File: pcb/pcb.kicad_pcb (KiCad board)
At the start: 2 copper layers, 60 x 30 mm, 54 parts, among them J1 USB_B_Mini, J2 I2C_BUS, J4 UART_BUS, Q1 BSS138DW-7-F, Q2 BSS138DW-7-F, SW1 PTS645Vx83, SW2 PTS645Vx83, SW3 PTS645Vx83, SW4 KMR2, U1 AP2112K-3.3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

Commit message: WIP
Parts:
- moved C6 0.80 mm to (58.8, 81.8)
- moved R14 0.80 mm to (60.8, 81.8)
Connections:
- U5 pad 10: nFAC_RST -> (no net)
- U5 pad 14: nINT -> (no net)
- U5 pad 17: (no net) -> nINT
- U5 pad 5: (no net) -> nFAC_RST
- U5 pad 6: (no net) -> RGB_LED
- U5 pad 9: RGB_LED -> (no net)
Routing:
- net UART_RX: track 55.2 -> 0.00 mm, vias 2 -> 0
- net UART_TX: track 53.3 -> 0.00 mm, vias 2 -> 0
- net nFAC_RST: track 11.3 -> 23.5 mm
- net nINT: track 12.1 -> 0.96 mm
- net RGB_LED: track 8.59 -> 15.3 mm, vias 0 -> 2

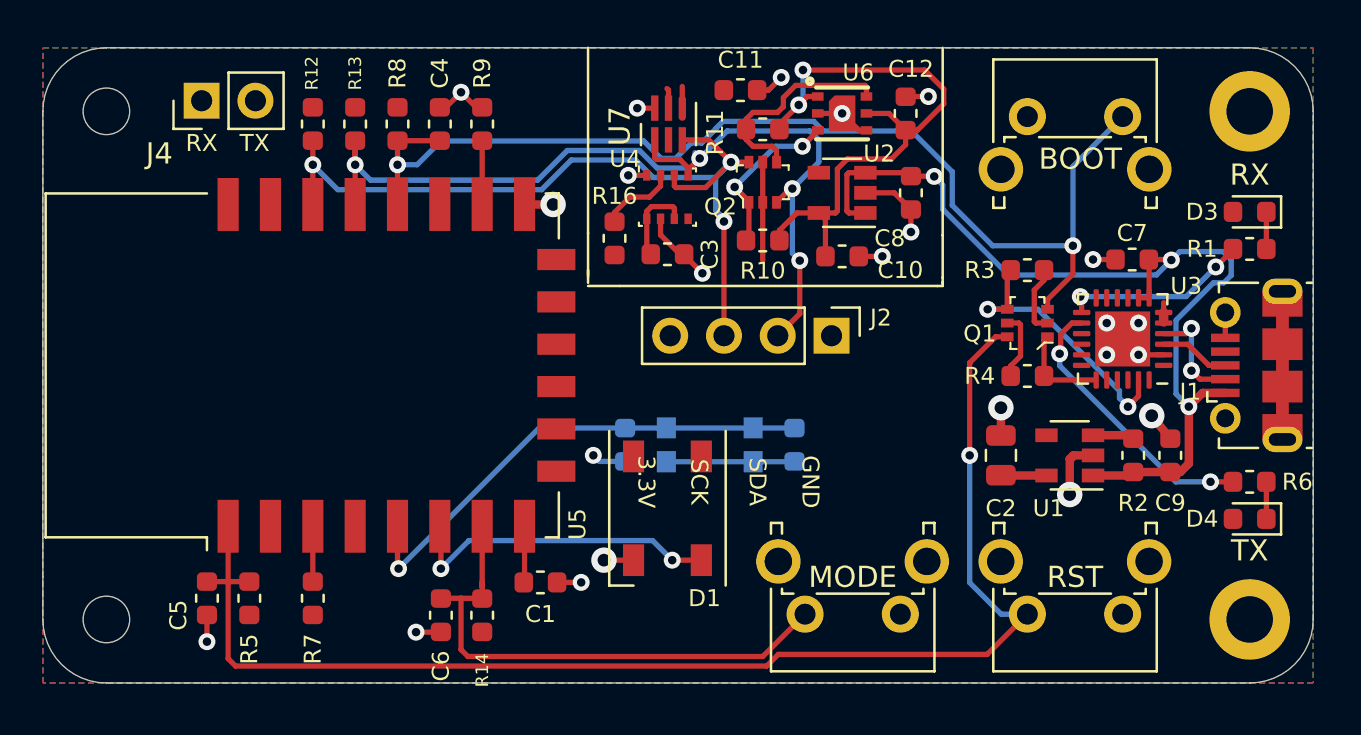
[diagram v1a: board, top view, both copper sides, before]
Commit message: Update the gerbers for the rem v1 and reroute the UART lines
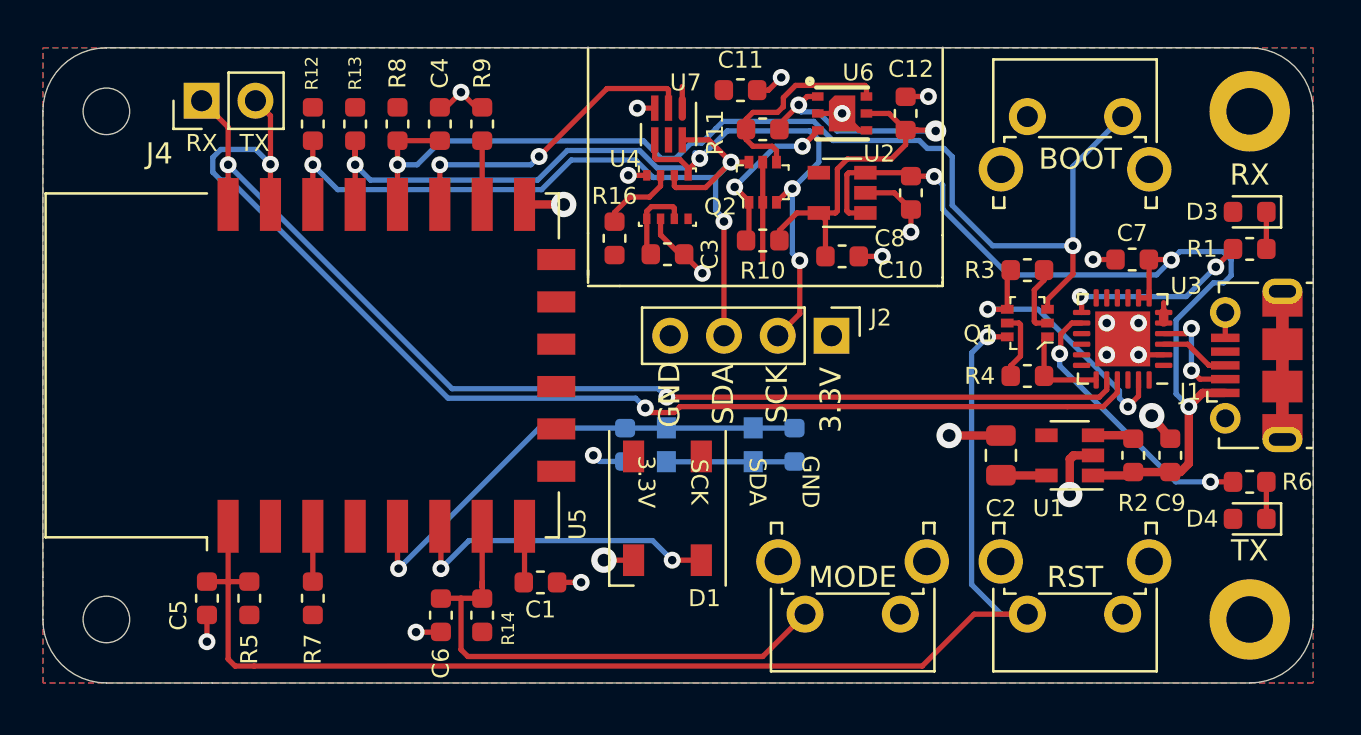
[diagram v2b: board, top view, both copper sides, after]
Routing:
- net UART_TX: track 0.00 -> 57.5 mm, vias 0 -> 2
- net UART_RX: track 0.00 -> 52.1 mm, vias 0 -> 2
- net nINT: track 0.96 -> 15.5 mm, vias 0 -> 2
- net +1V8: track 29.1 -> 26.7 mm
- net GND: track 46.8 -> 48.4 mm
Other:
- board text added: "FACTORY RST"
- board text added: "Route: 0.250mm signal, 0.4mm power. Grid: < 0.1270 mm Place Grid: 0.2 - 0.25 mm Vias: 0.8/0.4 signal, 1.2/0.6 power. Grid: < 0.1270"
- board text removed: "FAC_RST"

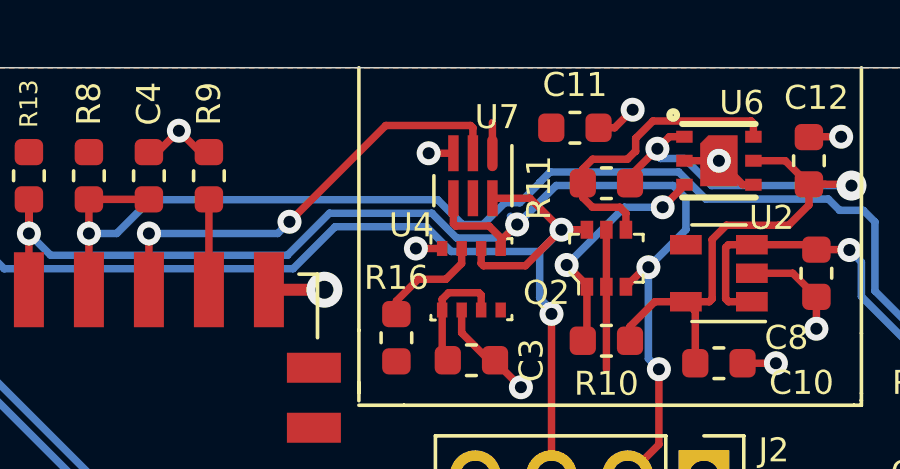
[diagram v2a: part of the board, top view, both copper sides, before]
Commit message: fix tsl2691 component
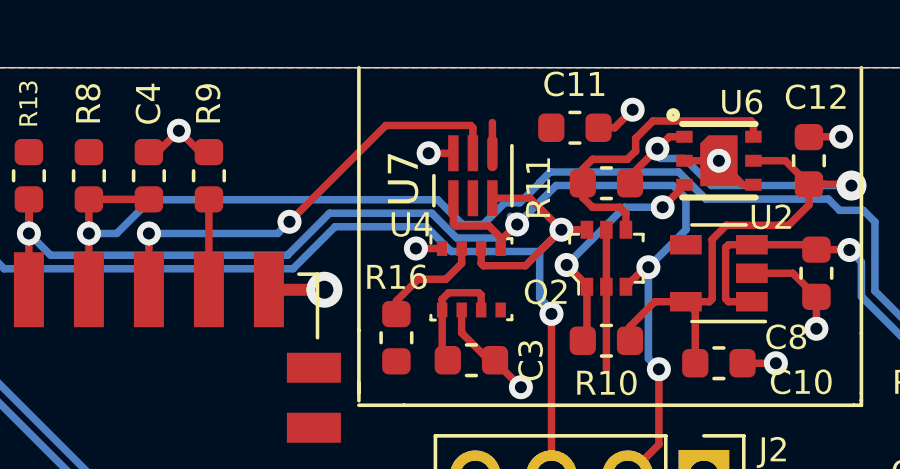
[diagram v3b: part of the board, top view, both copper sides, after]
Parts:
- U7: footprint Kevin-Lutzer-Kicad-Lbr:TSL2591 -> TSL2591:TSL2591
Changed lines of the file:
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@@
     (add_net I2C_SDA)
     (add_net I2C_SDA_1V8)
+    (add_net "Net-(D1-Pad2)")
     (add_net "Net-(D3-Pad1)")
     (add_net "Net-(D4-Pad1)")
+    (add_net "Net-(H1-Pad1)")
+    (add_net "Net-(H4-Pad1)")
     (add_net "Net-(J1-Pad2)")
     (add_net "Net-(J1-Pad3)")
+    (add_net "Net-(J1-Pad4)")
     (add_net "Net-(Q1-Pad1)")
     (add_net "Net-(Q1-Pad2)")
@@
     (add_net "Net-(R7-Pad2)")
     (add_net "Net-(R9-Pad1)")
+    (add_net "Net-(U1-Pad4)")
+    (add_net "Net-(U2-Pad4)")
+    (add_net "Net-(U3-Pad1)")
+    (add_net "Net-(U3-Pad10)")
+    (add_net "Net-(U3-Pad11)")
+    (add_net "Net-(U3-Pad12)")
+    (add_net "Net-(U3-Pad15)")
+    (add_net "Net-(U3-Pad16)")
+    (add_net "Net-(U3-Pad17)")
+    (add_net "Net-(U3-Pad18)")
+    (add_net "Net-(U3-Pad22)")
+    (add_net "Net-(U3-Pad24)")
+    (add_net "Net-(U3-Pad9)")
+    (add_net "Net-(U4-Pad5)")
+    (add_net "Net-(U5-Pad10)")
+    (add_net "Net-(U5-Pad11)")
+    (add_net "Net-(U5-Pad12)")
+    (add_net "Net-(U5-Pad13)")
+    (add_net "Net-(U5-Pad14)")
+    (add_net "Net-(U5-Pad2)")
+    (add_net "Net-(U5-Pad4)")
+    (add_net "Net-(U5-Pad9)")
+    (add_net "Net-(U7-Pad5)")
     (add_net RGB_LED)
     (add_net UART_RX)
@@
     (add_net nMODE)
     (add_net nRST)
+  )
+  (module TSL2591:TSL2591 (layer F.Cu)
+    (at 69.55 58.6 270)
+    (fp_text reference U7 (at 0.1 2.3 90) (layer F.SilkS)
+      (effects (font (size 1 1) (thickness 0.15)))
+    )
+    (fp_text value TSL2591 (at 0 -2.2 90) (layer F.Fab)
+      (effects (font (size 1 1) (thickness 0.15)))
+    )
+    (fp_line (start -1.5 -1.5) (end 1.5 -1.5) (layer F.CrtYd) (width 0.06))
+    (fp_line (start -1.5 1.5) (end -1.5 -1.5) (layer F.CrtYd) (width 0.06))
+    (fp_line (start 1.5 1.5) (end -1.5 1.5) (layer F.CrtYd) (width 0.06))
+    (fp_line (start 1.5 -1.5) (end 1.5 1.5) (layer F.CrtYd) (width 0.06))
+    (fp_line (start 1 1.3) (end 0 1.3) (layer F.SilkS) (width 0.12))
+    (fp_line (start 1 -1.3) (end -1 -1.3) (layer F.SilkS) (width 0.12))
+    (fp_line (start 1 1.2) (end 1 1) (layer F.Fab) (width 0.12))
+    (fp_line (start -1 1.2) (end 1 1.2) (layer F.Fab) (width 0.12))
+    (fp_line (start -1 1) (end -1 1.2) (layer F.Fab) (width 0.12))
+    (fp_line (start -1 -1) (end -1 1) (layer F.Fab) (width 0.12))
+    (fp_line (start -1 -1.2) (end -1 -1) (layer F.Fab) (width 0.12))
+    (fp_line (start 1 -1.2) (end -1 -1.2) (layer F.Fab) (width 0.12))
+    (fp_line (start 1 -1) (end 1 -1.2) (layer F.Fab) (width 0.12))
+    (fp_line (start -1 -1.2) (end 0 -1.2) (layer F.Fab) (width 0.12))
+    (fp_line (start -1 1) (end -1 -1) (layer F.Fab) (width 0.12))
+    (fp_line (start 1 1.2) (end -1 1.2) (layer F.Fab) (width 0.12))
+    (fp_line (start 1 -1) (end 1 1) (layer F.Fab) (width 0.12))
+    (fp_line (start 0 -1.2) (end 1 -1.2) (layer F.Fab) (width 0.12))
+    (pad 6 smd rect (at 0.75 -0.65 270) (size 1.2 0.35) (layers F.Cu F.Paste F.Mask)
+      (net 8 I2C_SDA))
+    (pad 5 smd rect (at 0.75 0 270) (size 1.2 0.35) (layers F.Cu F.Paste F.Mask))
+    (pad 4 smd rect (at 0.75 0.65 270) (size 1.2 0.35) (layers F.Cu F.Paste F.Mask)
+      (net 9 I2C_SCK))
+    (pad 3 smd rect (at -0.75 0.65 270) (size 1.2 0.35) (layers F.Cu F.Paste F.Mask)
+      (net 2 GND))
+    (pad 2 smd rect (at -0.75 0 270) (size 1.2 0.35) (layers F.Cu F.Paste F.Mask)
+      (net 19 nINT))
+    (pad 1 smd oval (at -0.75 -0.65 270) (size 1.2 0.35) (layers F.Cu F.Paste F.Mask)
+      (net 3 +3V3))
   )
   (module Connector_PinHeader_2.54mm:PinHeader_1x02_P2.54mm_Vertical (layer F.Cu)
@@
     )
   )
-  (module Kevin-Lutzer-Kicad-Lbr:TSL2591 (layer F.Cu)
-    (at 69.55 58.6 270)
-    (fp_text reference U7 (at -1.958 -0.808 180) (layer F.SilkS)
-      (effects (font (size 0.8 0.8) (thickness 0.12)))
-    )
-    (fp_text value TSL2591 (at 0 -2.2 90) (layer F.Fab)
-      (effects (font (size 1 1) (thickness 0.15)))
-    )
-    (fp_line (start 0 -1.2) (end 1 -1.2) (layer F.Fab) (width 0.12))
-    (fp_line (start 1 -1) (end 1 1) (layer F.Fab) (width 0.12))
-    (fp_line (start 1 1.2) (end -1 1.2) (layer F.Fab) (width 0.12))
-    (fp_line (start -1 1) (end -1 -1) (layer F.Fab) (width 0.12))
-    (fp_line (start -1 -1.2) (end 0 -1.2) (layer F.Fab) (width 0.12))
-    (fp_line (start 1 -1) (end 1 -1.2) (layer F.Fab) (width 0.12))
-    (fp_line (start 1 -1.2) (end -1 -1.2) (layer F.Fab) (width 0.12))
-    (fp_line (start -1 -1.2) (end -1 -1) (layer F.Fab) (width 0.12))
-    (fp_line (start -1 -1) (end -1 1) (layer F.Fab) (width 0.12))
-    (fp_line (start -1 1) (end -1 1.2) (layer F.Fab) (width 0.12))
-    (fp_line (start -1 1.2) (end 1 1.2) (layer F.Fab) (width 0.12))
-    (fp_line (start 1 1.2) (end 1 1) (layer F.Fab) (width 0.12))
-    (fp_line (start 1 -1.3) (end -1 -1.3) (layer F.SilkS) (width 0.12))
-    (fp_line (start 1 1.3) (end 0 1.3) (layer F.SilkS) (width 0.12))
-    (fp_line (start 1.5 -1.5) (end 1.5 1.5) (layer F.CrtYd) (width 0.06))
-    (fp_line (start 1.5 1.5) (end -1.5 1.5) (layer F.CrtYd) (width 0.06))
-    (fp_line (start -1.5 1.5) (end -1.5 -1.5) (layer F.CrtYd) (width 0.06))
-    (fp_line (start -1.5 -1.5) (end 1.5 -1.5) (layer F.CrtYd) (width 0.06))
-    (pad 1 smd oval (at -0.75 -0.65 270) (size 1.2 0.35) (layers F.Cu)
-      (net 3 +3V3))
-    (pad 2 smd rect (at -0.75 0 270) (size 1.2 0.35) (layers F.Cu)
-      (net 19 nINT))
-    (pad 3 smd rect (at -0.75 0.65 270) (size 1.2 0.35) (layers F.Cu)
-      (net 2 GND))
-    (pad 4 smd rect (at 0.75 0.65 270) (size 1.2 0.35) (layers F.Cu)
-      (net 9 I2C_SCK))
-    (pad 5 smd rect (at 0.75 0 270) (size 1.2 0.35) (layers F.Cu))
-    (pad 6 smd rect (at 0.75 -0.65 270) (size 1.2 0.35) (layers F.Cu)
-      (net 8 I2C_SDA))
-  )
   (gr_text 3.3V (at 77.216 71.628 90) (layer F.SilkS)
     (effects (font (size 1 1) (thickness 0.15)))
@@
   (segment (start 67.5 74.5375) (end 66.2875 74.5375) (width 0.25) (layer B.Cu) (net 3) (status 10))
   (segment (start 92.9375 67.5) (end 92.9375 67.94999) (width 0.45) (layer F.Cu) (net 3) (status 30))
-  (via (at 82.169 58.928) (size 1) (drill 0.4) (layers F.Cu B.Cu) (net 11))
   (via (at 68.453 72.009) (size 0.8) (drill 0.4) (layers F.Cu B.Cu) (net 4))
-  (via (at 84.625 68.65) (size 0.8) (drill 0.4) (layers F.Cu B.Cu) (net 6))
-  (via (at 58.75 60.525) (size 0.8) (drill 0.4) (layers F.Cu B.Cu) (net 19))
   (segment (start 50.75 58.21) (end 50.04 57.5) (width 0.25) (layer F.Cu) (net 4))
   (segment (start 50.75 62.4) (end 50.75 60.502) (width 0.25) (layer F.Cu) (net 4))
@@
   (segment (start 69.069001 71.101001) (end 59.326001 71.101001) (width 0.25) (layer B.Cu) (net 5))
   (segment (start 69.469 71.501) (end 69.069001 71.101001) (width 0.25) (layer B.Cu) (net 5))
+  (via (at 84.625 68.65) (size 0.8) (drill 0.4) (layers F.Cu B.Cu) (net 6))
   (segment (start 85.55 68.65) (end 84.625 68.65) (width 0.25) (layer F.Cu) (net 6))
   (segment (start 85.262564 81.75) (end 86.5 81.75) (width 0.25) (layer B.Cu) (net 6))
@@
   (segment (start 60.125001 78.274999) (end 58.8 79.6) (width 0.25) (layer B.Cu) (net 10))
   (segment (start 69.725001 79.2) (end 68.8 78.274999) (width 0.25) (layer B.Cu) (net 10))
+  (via (at 82.169 58.928) (size 1) (drill 0.4) (layers F.Cu B.Cu) (net 11))
   (segment (start 77.52499 62.70501) (end 77.52499 60.72501) (width 0.25) (layer F.Cu) (net 11))
   (segment (start 77.43 62.8) (end 77.52499 62.70501) (width 0.25) (layer F.Cu) (net 11))
@@
   (segment (start 74.6 59.65) (end 72.675 61.575) (width 0.25) (layer B.Cu) (net 18))
   (segment (start 75.875 59.65) (end 74.6 59.65) (width 0.25) (layer B.Cu) (net 18))
+  (via (at 58.75 60.525) (size 0.8) (drill 0.4) (layers F.Cu B.Cu) (net 19))
   (segment (start 58.75 62.4) (end 58.75 60.35301) (width 0.25) (layer F.Cu) (net 19))
   (segment (start 58.75 60.35301) (end 58.75 60.525) (width 0.25) (layer F.Cu) (net 19))

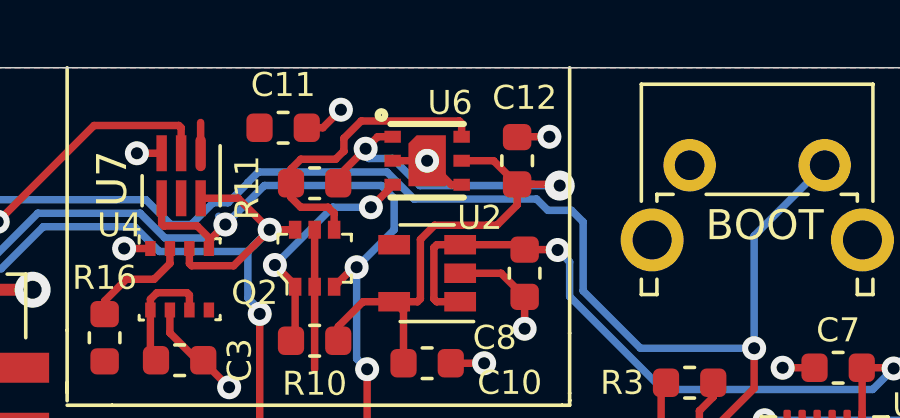
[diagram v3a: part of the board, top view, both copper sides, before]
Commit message: add more comments to the pcb, cleanup board files
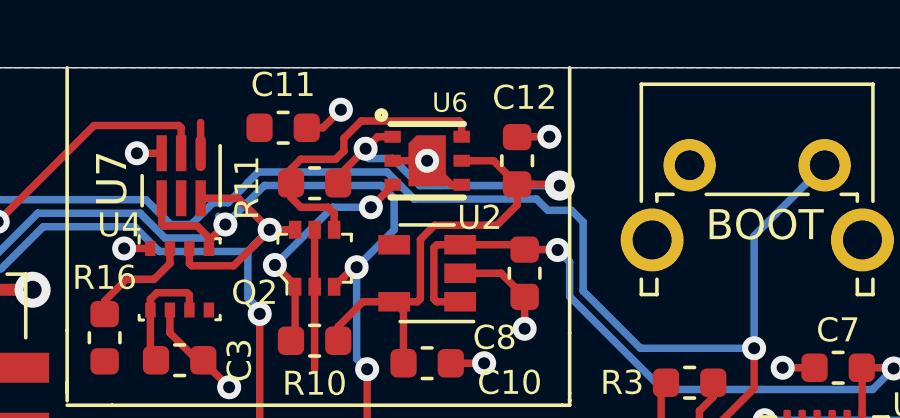
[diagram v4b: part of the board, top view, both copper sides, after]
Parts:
- U6: footprint SGP30 (1):SGP30 -> Kevin-Lutzer-Kicad-Lbr:SGP30
- U7: footprint TSL2591:TSL2591 -> Kevin-Lutzer-Kicad-Lbr:TSL2591
